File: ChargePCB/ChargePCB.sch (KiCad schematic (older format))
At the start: 38 parts, among them J1 Conn_01x01_Male, J2 Conn_01x01_Male, J3 USB_A, SW1 SW_SPDT, U1 LT3652, U2 S-8261, U3 DMG6968UDM, U4 RT4812

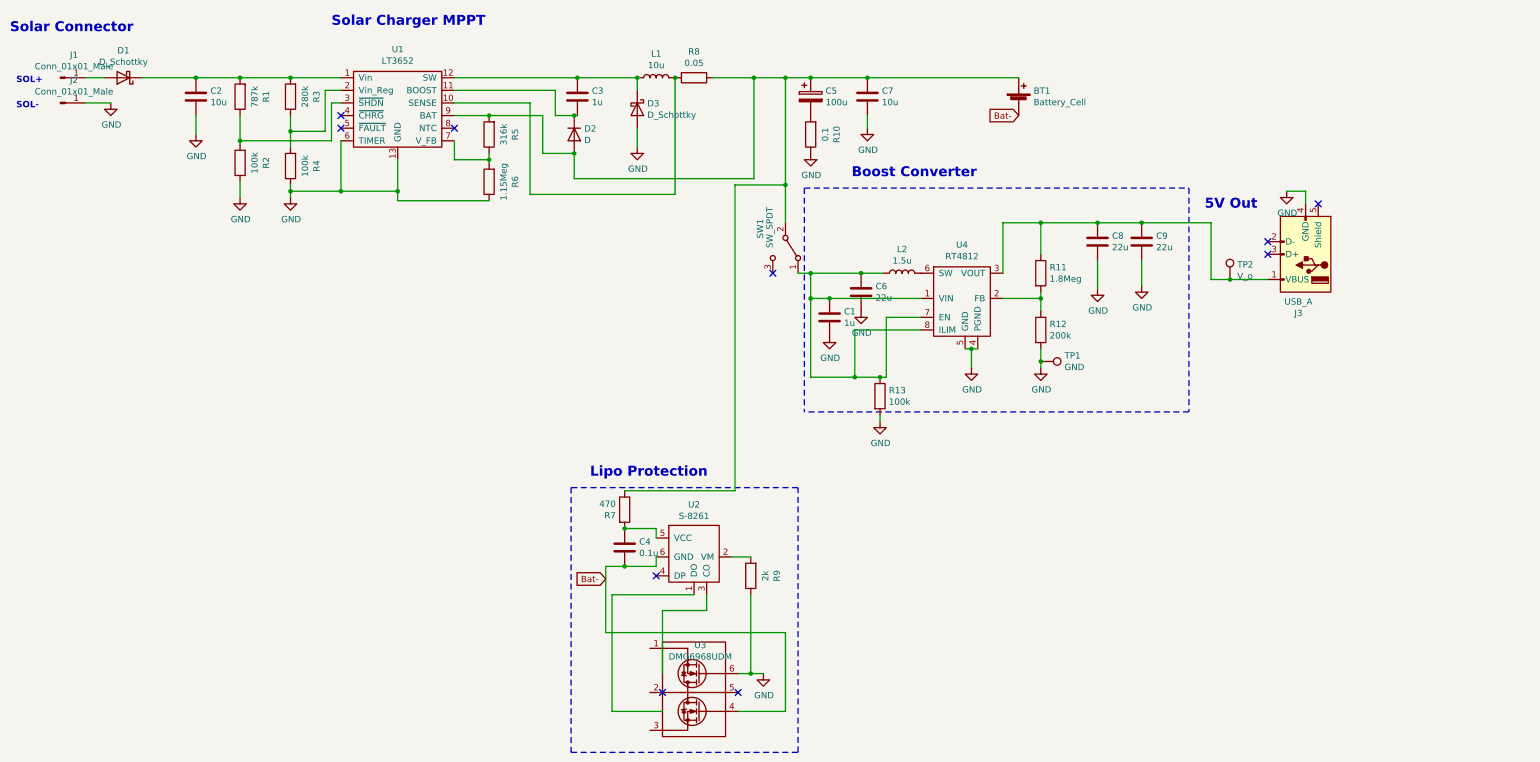
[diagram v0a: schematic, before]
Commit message: Fixing USB polarity, Lipo Protection, and 1.5uH footprint error
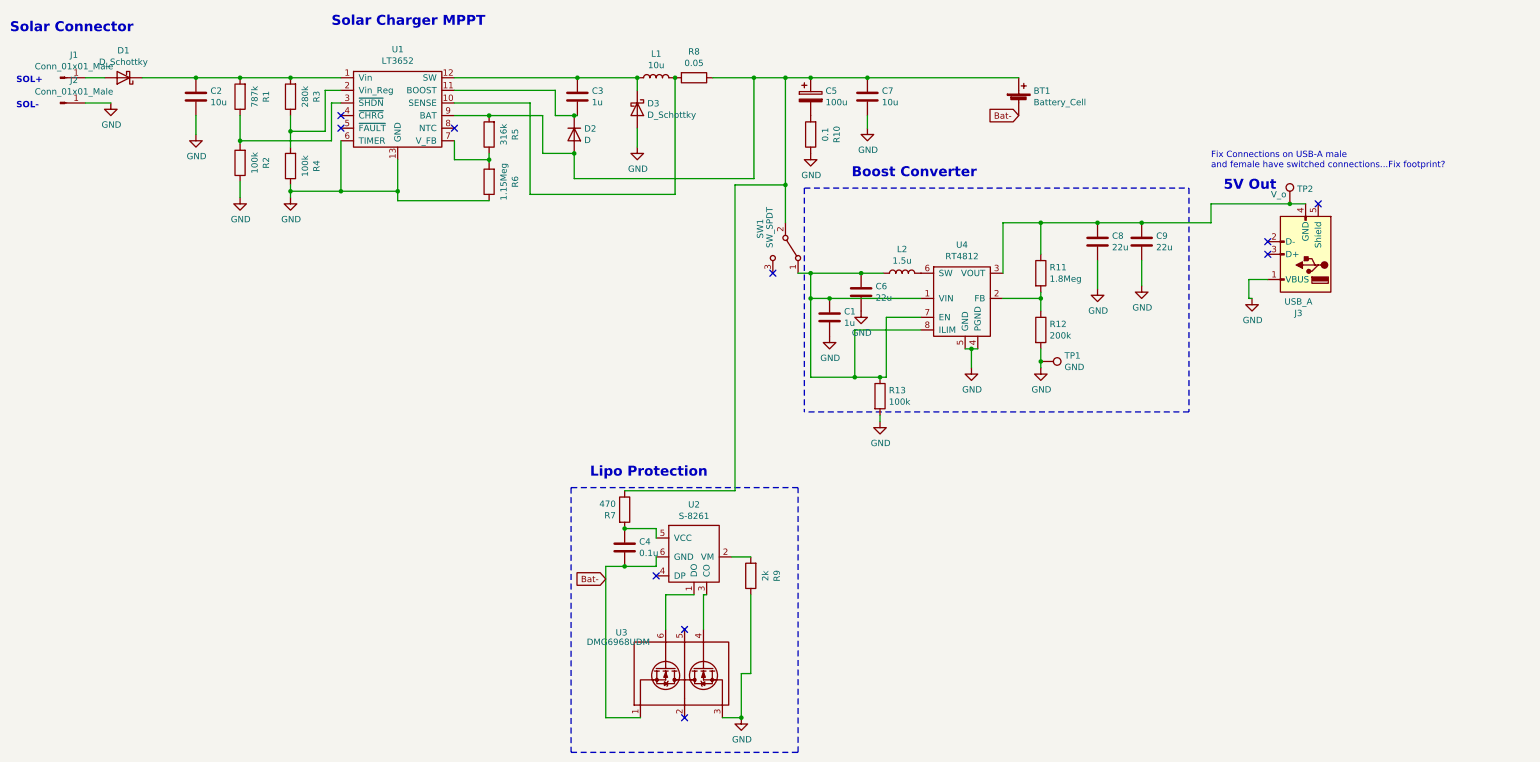
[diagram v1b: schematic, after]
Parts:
- L2: footprint Inductor_SMD:L_0805_2012Metric -> Inductor_SMD:L_Bourns-SRN6028
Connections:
- net Bat-: now also U3.1; no longer U3.4
- net GND: now also J3.1 (VBUS), U3.3; no longer J3.4 (GND), U3.6
- net at C8.1, C9.1, R11.1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: now also J3.4 (GND); no longer J3.1 (VBUS)
- net at U2.1 (DO): now also U3.6
- net at U2.3 (CO): now also U3.4
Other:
- note added: "Fix Connections on USB-A male \nand female have switched connections...Fix footprint?"
- moved on the sheet: TP2, U3
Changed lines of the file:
@@
 F 0 "L2" V 7840 3900 50  0000 C CNN
 F 1 "1.5u" V 7749 3900 50  0000 C CNN
-F 2 "Inductor_SMD:L_0805_2012Metric" H 7650 3900 50  0001 C CNN
-F 3 "${KIPRJMOD}\\Datasheets\\22uH-Inductor.pdf" H 7650 3900 50  0001 C CNN
+F 2 "Inductor_SMD:L_Bourns-SRN6028" H 7650 3900 50  0001 C CNN
+F 3 "${KIPRJMOD}\\Datasheets\\1.5uH-Inductor.pdf" H 7650 3900 50  0001 C CNN
 	1    7650 3900
 	0    -1   -1   0
@@
 Wire Wire Line
 	9550 4000 9550 3800
-Wire Wire Line
-	10550 3950 10250 3950
-Wire Wire Line
-	10100 3950 10100 3500
-$Comp
-L power:GND #PWR0105
-U 1 1 5CD654A1
-P 10700 3250
-F 0 "#PWR0105" H 10700 3000 50  0001 C CNN
-F 1 "GND" H 10705 3077 50  0000 C CNN
-F 2 "" H 10700 3250 50  0001 C CNN
-F 3 "" H 10700 3250 50  0001 C CNN
-	1    10700 3250
-	1    0    0    -1
-$EndComp
-Wire Wire Line
-	10700 3250 10850 3250
-Wire Wire Line
-	10850 3250 10850 3350
 NoConn ~ 10950 3350
 NoConn ~ 10550 3650
@@
 L Connector:TestPoint TP2
 U 1 1 5CD66D36
-P 10250 3950
-F 0 "TP2" H 10308 4068 50  0000 L CNN
-F 1 "V_o" H 10308 3977 50  0000 L CNN
-F 2 "TestPoint:TestPoint_Plated_Hole_D2.0mm" H 10450 3950 50  0001 C CNN
-F 3 "~" H 10450 3950 50  0001 C CNN
-	1    10250 3950
-	1    0    0    -1
-$EndComp
-Connection ~ 10250 3950
-Wire Wire Line
-	10250 3950 10100 3950
+P 10725 3350
+F 0 "TP2" H 10783 3468 50  0000 L CNN
+F 1 "V_o" H 10575 3425 50  0000 L CNN
+F 2 "TestPoint:TestPoint_Plated_Hole_D2.0mm" H 10925 3350 50  0001 C CNN
+F 3 "~" H 10925 3350 50  0001 C CNN
+	1    10725 3350
+	1    0    0    -1
+$EndComp
 $Comp
 L Connector:TestPoint TP1
@@
 Wire Wire Line
 	8750 4600 8750 4650
-Text Notes 10050 3400 0    79   ~ 16
+Text Notes 10200 3250 0    79   ~ 16
 5V Out
 $Comp
@@
 Wire Wire Line
 	6450 6150 6300 6150
-Wire Wire Line
-	5750 7375 5350 7375
-Wire Wire Line
-	5350 7375 5350 6450
-Wire Wire Line
-	5350 6450 6000 6450
-Wire Wire Line
-	5750 7075 5750 6575
-Wire Wire Line
-	5750 6575 6100 6575
-Wire Wire Line
-	6100 6575 6100 6450
-NoConn ~ 6350 7225
-NoConn ~ 5750 7225
-Wire Wire Line
-	6350 7375 6725 7375
-Wire Wire Line
-	6725 7375 6725 6750
 $Comp
 L power:GND #PWR0110
 U 1 1 5CE0BB7C
-P 6550 7075
-F 0 "#PWR0110" H 6550 6825 50  0001 C CNN
-F 1 "GND" H 6555 6902 50  0000 C CNN
-F 2 "" H 6550 7075 50  0001 C CNN
-F 3 "" H 6550 7075 50  0001 C CNN
-	1    6550 7075
-	1    0    0    -1
-$EndComp
-Wire Wire Line
-	6550 7075 6450 7075
-Wire Wire Line
-	5450 6225 5700 6225
+P 6375 7425
+F 0 "#PWR0110" H 6375 7175 50  0001 C CNN
+F 1 "GND" H 6380 7252 50  0000 C CNN
+F 2 "" H 6375 7425 50  0001 C CNN
+F 3 "" H 6375 7425 50  0001 C CNN
+	1    6375 7425
+	1    0    0    -1
+$EndComp
 Wire Wire Line
 	5450 6225 5300 6225
 Connection ~ 5450 6225
 Wire Wire Line
-	5300 6750 6725 6750
-Wire Wire Line
-	5300 6225 5300 6750
-Wire Wire Line
 	6450 6450 6450 7075
-Connection ~ 6450 7075
-Wire Wire Line
-	6450 7075 6350 7075
 Text Notes 5175 5525 0    79   ~ 16
 Lipo Protection
@@
 L Proj:DMG6968UDM U3
 U 1 1 5CE3DD74
-P 6050 7225
-F 0 "U3" H 6050 7600 50  0000 C CNN
-F 1 "DMG6968UDM" H 6050 7509 50  0000 C CNN
-F 2 "Package_TO_SOT_SMD:SOT-23-6" H 6050 7225 50  0001 C CNN
-F 3 "${KIPRJMOD}\\Datasheets\\DMG6968UDM.pdf" H 6050 7225 50  0001 C CNN
-	1    6050 7225
-	1    0    0    -1
+P 5925 7025
+F 0 "U3" V 6200 7525 50  0000 C CNN
+F 1 "DMG6968UDM" V 6125 7550 50  0000 C CNN
+F 2 "Package_TO_SOT_SMD:SOT-23-6" H 5925 7025 50  0001 C CNN
+F 3 "${KIPRJMOD}\\Datasheets\\DMG6968UDM.pdf" H 5925 7025 50  0001 C CNN
+	1    5925 7025
+	0    -1   -1   0
 $EndComp
 $Comp
@@
 Wire Wire Line
 	9550 3500 10100 3500
+Text Notes 10100 3075 0    50   ~ 0
+Fix Connections on USB-A male \nand female have switched connections...Fix footprint?
+NoConn ~ 5925 6725
+Wire Wire Line
+	5300 6225 5300 7425
+Wire Wire Line
+	5300 7425 5575 7425
+Wire Wire Line
+	5775 6725 5775 6450
+Wire Wire Line
+	5775 6450 6000 6450
+Wire Wire Line
+	6075 6725 6075 6450
+Wire Wire Line
+	6075 6450 6100 6450
+Wire Wire Line
+	6225 7425 6375 7425
+Wire Wire Line
+	6450 7075 6375 7075
+Wire Wire Line
+	6375 7075 6375 7425
+Connection ~ 6375 7425
+Wire Wire Line
+	5450 6225 5700 6225
+Wire Wire Line
+	10850 3350 10725 3350
+Wire Wire Line
+	10100 3350 10100 3500
+Connection ~ 10725 3350
+Wire Wire Line
+	10725 3350 10100 3350
+Wire Wire Line
+	10550 3950 10400 3950
+Wire Wire Line
+	10400 3950 10400 4100
+Wire Wire Line
+	10400 4100 10425 4100
+$Comp
+L power:GND #PWR0105
+U 1 1 5CF728B7
+P 10425 4100
+F 0 "#PWR0105" H 10425 3850 50  0001 C CNN
+F 1 "GND" H 10430 3927 50  0000 C CNN
+F 2 "" H 10425 4100 50  0001 C CNN
+F 3 "" H 10425 4100 50  0001 C CNN
+	1    10425 4100
+	1    0    0    -1
+$EndComp
+NoConn ~ 5925 7425
 $EndSCHEMATC
